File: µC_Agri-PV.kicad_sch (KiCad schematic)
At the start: 0 parts

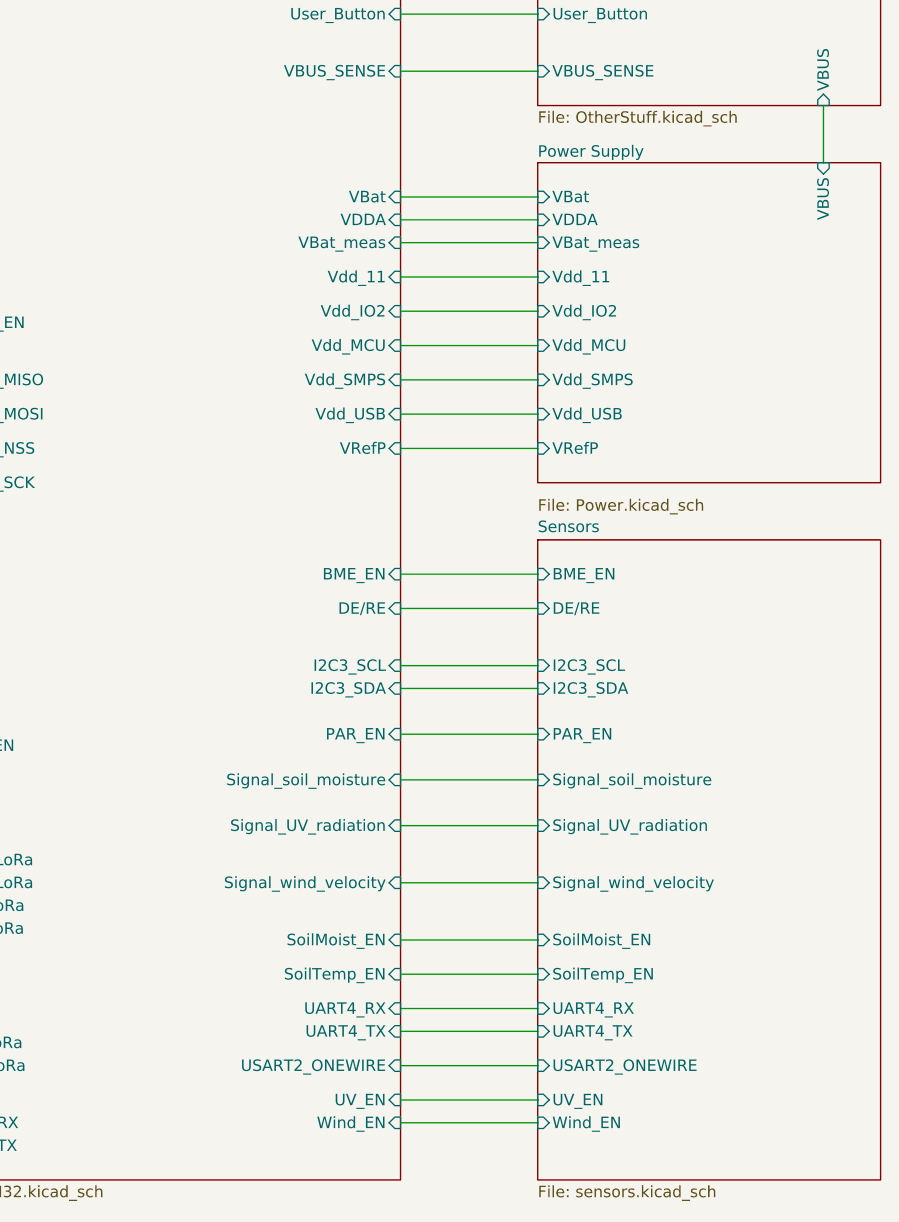
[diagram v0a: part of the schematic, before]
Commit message: Add TP4056-18650 footprint and update Power schematic
Added the TP4056-18650-2 footprint to the library and assigned it to the battery charger in Power.kicad_sch. Updated the Power schematic to improve symbol details, add descriptive properties, and enhance the 3V3 lane toggling section. Made various net and annotation adjustments, and removed obsolete autosave and lock files.
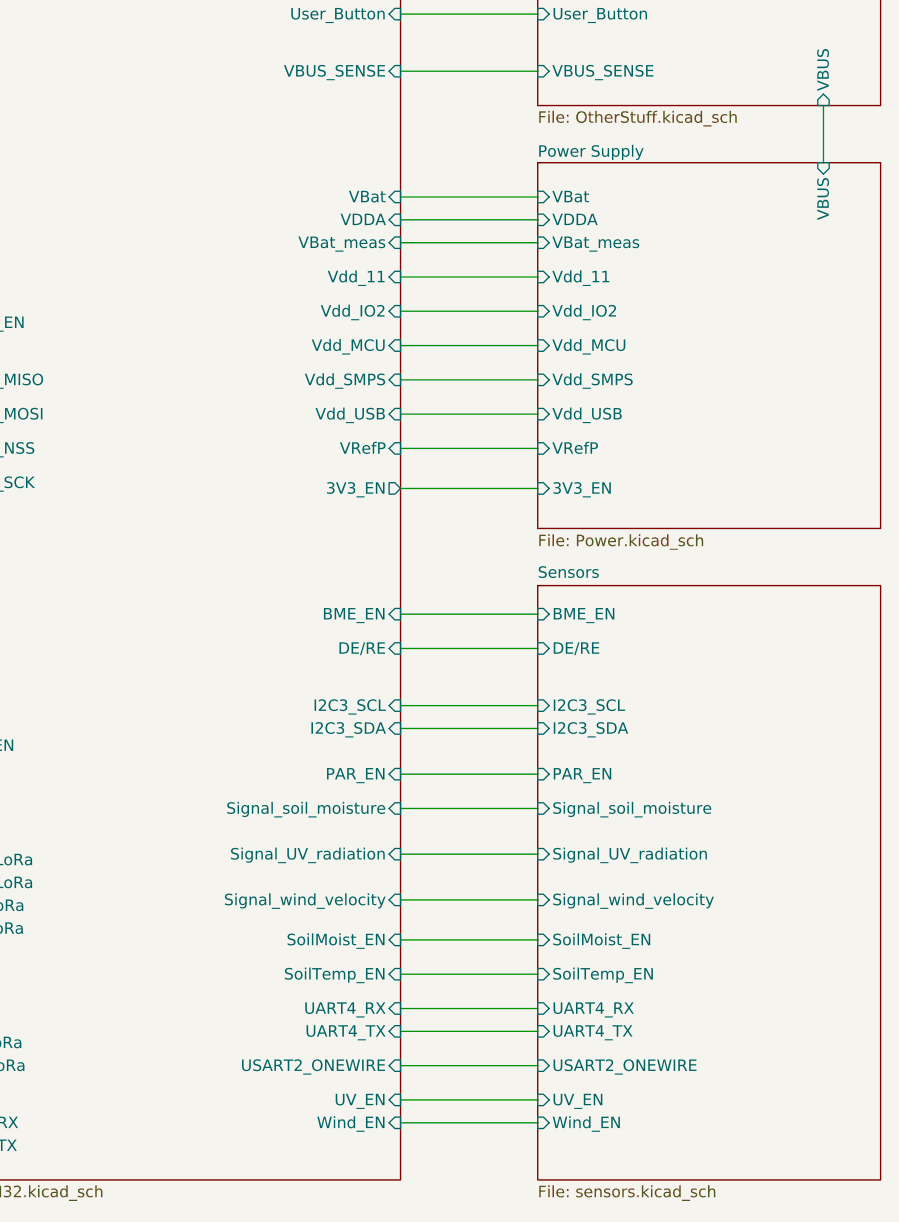
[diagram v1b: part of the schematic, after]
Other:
- sheet Power Supply ports: added 3V3_EN; removed none
- sheet STM32U575ZIT6Q ports: added 3V3_EN; removed none
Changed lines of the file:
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@@
 	(wire
 		(pts
-			(xy 132.08 165.1) (xy 147.32 165.1)
+			(xy 132.08 169.545) (xy 147.32 169.545)
 		)
 		(stroke
@@
 	(wire
 		(pts
-			(xy 132.08 154.94) (xy 147.32 154.94)
+			(xy 132.08 159.385) (xy 147.32 159.385)
 		)
 		(stroke
@@
 	(wire
 		(pts
-			(xy 132.08 172.72) (xy 147.32 172.72)
+			(xy 132.08 177.165) (xy 147.32 177.165)
 		)
 		(stroke
@@
 	(wire
 		(pts
+			(xy 132.08 145.415) (xy 147.32 145.415)
+		)
+		(stroke
+			(width 0)
+			(type default)
+		)
+	)
+	(wire
+		(pts
 			(xy 52.07 66.04) (xy 80.01 66.04)
 		)
@@
 	(wire
 		(pts
-			(xy 132.08 182.88) (xy 147.32 182.88)
+			(xy 132.08 186.055) (xy 147.32 186.055)
 		)
 		(stroke
@@
 	(wire
 		(pts
-			(xy 132.08 189.23) (xy 147.32 189.23)
-		)
-		(stroke
-			(width 0)
-			(type default)
-		)
-	)
-	(wire
-		(pts
-			(xy 132.08 167.64) (xy 147.32 167.64)
+			(xy 132.08 191.135) (xy 147.32 191.135)
+		)
+		(stroke
+			(width 0)
+			(type default)
+		)
+	)
+	(wire
+		(pts
+			(xy 132.08 172.085) (xy 147.32 172.085)
 		)
 		(stroke
@@
 	(wire
 		(pts
-			(xy 132.08 158.75) (xy 147.32 158.75)
+			(xy 132.08 163.195) (xy 147.32 163.195)
 		)
 		(stroke
@@
 	(wire
 		(pts
-			(xy 132.08 177.8) (xy 147.32 177.8)
+			(xy 132.08 180.975) (xy 147.32 180.975)
 		)
 		(stroke
@@
 	(sheet
 		(at 147.32 109.22)
-		(size 38.1 35.56)
+		(size 38.1 40.64)
 		(exclude_from_sim no)
 		(in_bom yes)
@@
 		)
 		(property "Sheetfile" "Power.kicad_sch"
-			(at 147.32 146.558 0)
+			(at 147.32 150.495 0)
 			(effects
 				(font
@@
 				)
 				(justify right)
+			)
+		)
+		(pin "3V3_EN" input
+			(at 147.32 145.415 180)
+			(effects
+				(font
+					(size 1.27 1.27)
+				)
+				(justify left)
 			)
 		)
@@
 		)
 		(pin "DE{slash}RE" input
-			(at 132.08 158.75 0)
+			(at 132.08 163.195 0)
 			(effects
 				(font
@@
 		)
 		(pin "I2C3_SCL" input
-			(at 132.08 165.1 0)
+			(at 132.08 169.545 0)
 			(effects
 				(font
@@
 		)
 		(pin "I2C3_SDA" input
-			(at 132.08 167.64 0)
+			(at 132.08 172.085 0)
 			(effects
 				(font
@@
 		)
 		(pin "Signal_soil_moisture" input
-			(at 132.08 177.8 0)
+			(at 132.08 180.975 0)
 			(effects
 				(font
@@
 		)
 		(pin "Signal_UV_radiation" input
-			(at 132.08 182.88 0)
+			(at 132.08 186.055 0)
 			(effects
 				(font
@@
 		)
 		(pin "Signal_wind_velocity" input
-			(at 132.08 189.23 0)
+			(at 132.08 191.135 0)
 			(effects
 				(font
@@
 		)
 		(pin "PAR_EN" input
-			(at 132.08 172.72 0)
+			(at 132.08 177.165 0)
 			(effects
 				(font
@@
 		)
 		(pin "BME_EN" input
-			(at 132.08 154.94 0)
+			(at 132.08 159.385 0)
 			(effects
 				(font
@@
 		(pin "Vdd_IO2" input
 			(at 132.08 125.73 0)
+			(effects
+				(font
+					(size 1.27 1.27)
+				)
+				(justify right)
+			)
+		)
+		(pin "3V3_EN" output
+			(at 132.08 145.415 0)
 			(effects
 				(font
@@
 	)
 	(sheet
-		(at 147.32 151.13)
-		(size 38.1 71.12)
+		(at 147.32 156.21)
+		(size 38.1 66.04)
 		(exclude_from_sim no)
 		(in_bom yes)
@@
 		)
 		(property "Sheetname" "Sensors"
-			(at 147.32 150.4184 0)
+			(at 147.32 155.4984 0)
 			(effects
 				(font
@@
 		)
 		(pin "BME_EN" input
-			(at 147.32 154.94 180)
+			(at 147.32 159.385 180)
 			(effects
 				(font
@@
 		)
 		(pin "DE{slash}RE" input
-			(at 147.32 158.75 180)
+			(at 147.32 163.195 180)
 			(effects
 				(font
@@
 		)
 		(pin "I2C3_SCL" input
-			(at 147.32 165.1 180)
+			(at 147.32 169.545 180)
 			(effects
 				(font
@@
 		)
 		(pin "I2C3_SDA" input
-			(at 147.32 167.64 180)
+			(at 147.32 172.085 180)
 			(effects
 				(font
@@
 		)
 		(pin "PAR_EN" input
-			(at 147.32 172.72 180)
+			(at 147.32 177.165 180)
 			(effects
 				(font
@@
 		)
 		(pin "Signal_soil_moisture" input
-			(at 147.32 177.8 180)
+			(at 147.32 180.975 180)
 			(effects
 				(font
@@
 		)
 		(pin "Signal_UV_radiation" input
-			(at 147.32 182.88 180)
+			(at 147.32 186.055 180)
 			(effects
 				(font
@@
 		)
 		(pin "Signal_wind_velocity" input
-			(at 147.32 189.23 180)
-			(effects
-				(font
+			(at 147.32 191.135 180)
+			(effects
+				(font
